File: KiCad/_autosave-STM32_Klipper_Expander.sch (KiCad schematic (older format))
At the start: 45 parts, among them J1 USB_B_Micro, J10 Conn_01x01, J11 Conn_01x03, J12 Conn_01x02, J2 Conn_01x04, J4 Conn_01x03, J5 Vin, J6 Screw_Terminal_01x08, J7 Conn_01x02, J8 Conn_01x02, J9 Conn_01x02, Q1 IRLML6344TRPBF, Q2 IRLML6344TRPBF, Q3 IRLML6344TRPBF, Q4 IRLML6344TRPBF, SW2 SW_SPST, U1 STM32F042F6Px, U2 AP2127K-3.3, U3 74LVC1G17

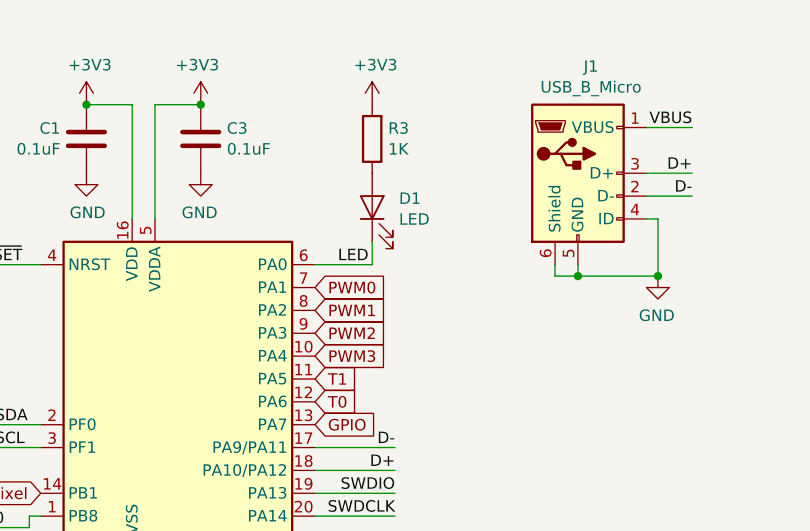
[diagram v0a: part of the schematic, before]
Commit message: Routing and finalizations
Completed routing on the thinner variant. Need to gerenate BOM and CPL files for JLCPCB assembly
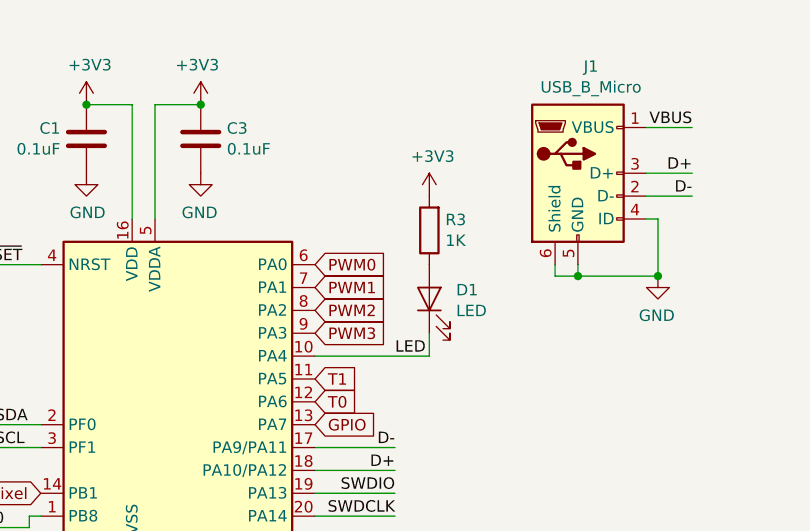
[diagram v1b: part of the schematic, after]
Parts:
- J1: footprint Connector_USB:USB_Micro-B_Molex_47346-0001 -> TRA_KiCad_Footprints:Molex-105017-0001-USBMicroB
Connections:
- net LED: now also U1.10 (PA4); no longer U1.6 (PA0)
- net PWM0: now also U1.6 (PA0); no longer U1.7 (PA1)
- net PWM1: now also U1.7 (PA1); no longer U1.8 (PA2)
- net PWM2: now also U1.8 (PA2); no longer U1.9 (PA3)
- net PWM3: now also U1.9 (PA3); no longer U1.10 (PA4)
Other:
- moved on the sheet: D1, R3
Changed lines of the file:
@@
 	1    0    0    -1
-$EndComp
-$Comp
-L power:+3V3 #PWR012
-U 1 1 5E207BBA
-P 2600 850
-F 0 "#PWR012" H 2600 700 50  0001 C CNN
-F 1 "+3V3" H 2615 1023 50  0000 C CNN
-F 2 "" H 2600 850 50  0001 C CNN
-F 3 "" H 2600 850 50  0001 C CNN
-	1    2600 850
-	1    0    0    -1
-$EndComp
-Wire Wire Line
-	2600 1550 2600 1450
-$Comp
-L Device:LED D1
-U 1 1 5E207BFA
-P 2600 1300
-F 0 "D1" V 2639 1183 50  0000 R CNN
-F 1 "LED" V 2548 1183 50  0000 R CNN
-F 2 "LED_SMD:LED_0805_2012Metric" H 2600 1300 50  0001 C CNN
-F 3 "~" H 2600 1300 50  0001 C CNN
-	1    2600 1300
-	0    -1   -1   0
-$EndComp
-$Comp
-L Device:R R3
-U 1 1 5E207C00
-P 2600 1000
-F 0 "R3" H 2530 954 50  0000 R CNN
-F 1 "1K" H 2530 1045 50  0000 R CNN
-F 2 "Resistor_SMD:R_0805_2012Metric" V 2530 1000 50  0001 C CNN
-F 3 "~" H 2600 1000 50  0001 C CNN
-	1    2600 1000
-	-1   0    0    1
 $EndComp
 Wire Wire Line
@@
 F 0 "J1" H 3557 1617 50  0000 C CNN
 F 1 "USB_B_Micro" H 3557 1526 50  0000 C CNN
-F 2 "Connector_USB:USB_Micro-B_Molex_47346-0001" H 3650 1100 50  0001 C CNN
+F 2 "TRA_KiCad_Footprints:Molex-105017-0001-USBMicroB" H 3650 1100 50  0001 C CNN
 F 3 "~" H 3650 1100 50  0001 C CNN
 	1    3500 1150
@@
 	10000 2650 10000 2000
 Connection ~ 10000 2650
+Text GLabel 2350 1550 2    50   Input ~ 0
+PWM0
 Text GLabel 2350 1650 2    50   Input ~ 0
-PWM0
+PWM1
 Text GLabel 2350 1750 2    50   Input ~ 0
-PWM1
+PWM2
 Text GLabel 2350 1850 2    50   Input ~ 0
-PWM2
-Text GLabel 2350 1950 2    50   Input ~ 0
 PWM3
-Wire Wire Line
-	2600 1550 2350 1550
-Text Label 2450 1550 0    50   ~ 0
-LED
 Wire Wire Line
 	1250 4550 1250 4600
@@
 	1    0    0    -1
 $EndComp
+$Comp
+L power:+3V3 #PWR012
+U 1 1 5E207BBA
+P 2850 1250
+F 0 "#PWR012" H 2850 1100 50  0001 C CNN
+F 1 "+3V3" H 2865 1423 50  0000 C CNN
+F 2 "" H 2850 1250 50  0001 C CNN
+F 3 "" H 2850 1250 50  0001 C CNN
+	1    2850 1250
+	1    0    0    -1
+$EndComp
+Wire Wire Line
+	2850 1950 2850 1850
+$Comp
+L Device:LED D1
+U 1 1 5E207BFA
+P 2850 1700
+F 0 "D1" V 2889 1583 50  0000 R CNN
+F 1 "LED" V 2798 1583 50  0000 R CNN
+F 2 "LED_SMD:LED_0805_2012Metric" H 2850 1700 50  0001 C CNN
+F 3 "~" H 2850 1700 50  0001 C CNN
+	1    2850 1700
+	0    -1   -1   0
+$EndComp
+$Comp
+L Device:R R3
+U 1 1 5E207C00
+P 2850 1400
+F 0 "R3" H 2780 1354 50  0000 R CNN
+F 1 "1K" H 2780 1445 50  0000 R CNN
+F 2 "Resistor_SMD:R_0805_2012Metric" V 2780 1400 50  0001 C CNN
+F 3 "~" H 2850 1400 50  0001 C CNN
+	1    2850 1400
+	-1   0    0    1
+$EndComp
+Wire Wire Line
+	2850 1950 2350 1950
+Text Label 2700 1950 0    50   ~ 0
+LED
 $EndSCHEMATC
